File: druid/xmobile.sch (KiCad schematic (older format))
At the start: 10 parts, among them P3 CONN_8

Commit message: some changes
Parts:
- added J?: TP_VIBRO, symbol TEST_2P
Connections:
- wire segments 69 -> 70
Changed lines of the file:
@@
 	0    1    1    0
 $EndComp
+$Comp
+L TEST_2P J?
+U 1 1 5C561693
+P 7300 7200
+F 0 "J?" H 7300 7260 50  0000 C CNN
+F 1 "TP_VIBRO" H 7300 7130 50  0000 C CNN
+F 2 "" H 7300 7200 50  0001 C CNN
+F 3 "" H 7300 7200 50  0001 C CNN
+	1    7300 7200
+	1    0    0    -1
+$EndComp
+Wire Wire Line
+	7500 7200 7800 7200
+Text Label 7100 7200 2    60   ~ 0
+GND
 $EndSCHEMATC

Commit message: Add some packages
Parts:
- removed J?: Conn_01x04, symbol Conn_01x04
- added W?: TEST_PDI, Measurement_Points:Test_Point_2Pads, symbol TEST
- added W?: TEST_XMEGA_PWR, Measurement_Points:Test_Point_2Pads, symbol TEST
- C?: footprint (none) -> Capacitors_SMD:C_0402; case (none) -> 0402 In; example (none) -> https://eu.mouser.com/ProductDetail/AVX/04026D104KAT4A?qs=s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
- C?: value 10-100u -> 33u; footprint (none) -> Capacitors_SMD:c_elec_5x5.3; case (none) -> 5x5,3mm; example (none) -> https://eu.mouser.com/ProductDetail/Panasonic/EEE-0JA330WR?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
- J?: value TP_DISP_DATA_OUT -> TEST_DISP_DATA_OUT; footprint (none) -> Measurement_Points:Measurement_Point_Square-TH_Small; case (none) -> 1 pad
- J?: value TP_VIBRO -> TEST_VIBRO; footprint (none) -> Measurement_Points:Test_Point_2Pads; case (none) -> 2 pads
- P3: footprint Connectors_JAE:JAE_LY20-08P-2T_2x04x2.00mm_Straight -> Pin_Headers:Pin_Header_Straight_1x08
- R6: footprint (none) -> Resistors_SMD:R_0402; case (none) -> 0402 In; example (none) -> https://eu.mouser.com/ProductDetail/ROHM-Semiconductor/SFR0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
- SW?: case (none) -> 4x4x0,8; example (none) -> https://ru.aliexpress.com/item/100-4-4-0-8/32909011951.html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
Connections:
- wire segments 70 -> 69
- no-connect marks 3 -> 25
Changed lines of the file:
@@
 F 0 "R6" V 10105 10100 40  0000 C CNN
 F 1 "10k" V 10032 10101 40  0000 C CNN
-F 2 "" V 9955 10100 30  0000 C CNN
-F 3 "" H 10025 10100 30  0000 C CNN
+F 2 "Resistors_SMD:R_0402" V 9955 10100 30  0001 C CNN
+F 3 "https://eu.mouser.com/datasheet/2/348/sfr-e-1507454.pdf" V 10200 9750 30  0001 C CNN
+F 4 "https://eu.mouser.com/ProductDetail/ROHM-Semiconductor/SFR01MZPJ103?qs=sGAEpiMZZMtlubZbdhIBIIR71ikvQRXLchgEzboAcvI%3d" V 10025 10100 60  0001 C CNN "example"
+F 5 "0402 In" V 9950 10100 30  0000 C CNN "case"
 	1    10025 10100
 	0    -1   -1   0
@@
 F 0 "P3" V 13475 7500 60  0000 C CNN
 F 1 "CONN_8" V 13575 7500 60  0000 C CNN
-F 2 "Connectors_JAE:JAE_LY20-08P-2T_2x04x2.00mm_Straight" H 13525 7500 60  0001 C CNN
+F 2 "Pin_Headers:Pin_Header_Straight_1x08" V 13700 7450 60  0000 C CNN
 F 3 "" H 13525 7500 60  0001 C CNN
-F 4 "EPD display connector" V 13700 7500 60  0000 C CNN "description"
+F 4 "EPD display connector" V 13700 7500 60  0001 C CNN "description"
 	1    13525 7500
 	1    0    0    -1
@@
 F1 "xmega_power.sch" 60
 $EndSheet
-Text Label 9650 10700 1    60   ~ 0
+Text Label 9725 10700 0    60   ~ 0
 3.3V
-Text Label 9450 10700 1    60   ~ 0
+Text Label 9325 10700 2    60   ~ 0
 GND
 Text Label 8700 10100 2    60   ~ 0
@@
 F4 "INT" O L 13125 6400 60
 $EndSheet
-Text Label 9975 10325 0    60   ~ 0
+Text Label 10100 10350 0    60   ~ 0
 PDI_D
 Text Label 9550 9950 1    60   ~ 0
@@
 Wire Wire Line
 	9300 10100 9775 10100
-Wire Wire Line
-	9550 9950 9550 10700
 Connection ~ 9550 10100
-Wire Wire Line
-	9750 10325 9750 10700
-Wire Wire Line
-	9750 10325 9975 10325
 Wire Wire Line
 	12875 4675 14025 4675
@@
 P 11625 4600
 F 0 "J?" H 11625 4870 50  0000 C CNN
-F 1 "TP_DISP_DATA_OUT" H 11625 4800 50  0000 C CNN
-F 2 "" H 11825 4600 50  0001 C CNN
+F 1 "TEST_DISP_DATA_OUT" H 11625 4800 50  0000 C CNN
+F 2 "Measurement_Points:Measurement_Point_Square-TH_Small" H 11650 4925 50  0001 C CNN
 F 3 "" H 11825 4600 50  0001 C CNN
+F 4 "1 pad" H 11625 4925 30  0000 C CNN "case"
 	1    11625 4600
 	0    1    1    0
@@
 P 1975 9100
 F 0 "C?" H 2000 9200 50  0000 L CNN
-F 1 "0.1u" H 2000 9000 50  0000 L CNN
-F 2 "" H 2150 9075 50  0000 C CNN
-F 3 "" H 1975 9100 50  0001 C CNN
+F 1 "0.1u" H 2100 9100 50  0000 L CNN
+F 2 "Capacitors_SMD:C_0402" H 2175 9375 50  0001 C CNN
+F 3 "https://eu.mouser.com/datasheet/2/40/cx5r-776519.pdf" H 1975 9100 50  0001 C CNN
+F 4 "https://eu.mouser.com/ProductDetail/AVX/04026D104KAT4A?qs=sGAEpiMZZMs0AnBnWHyRQPg4iYkCw7IMED%2f4kpqgf7w%3d" H 1975 9100 60  0001 C CNN "example"
+F 5 "0402 In" H 2100 9025 30  0000 C CNN "case"
 	1    1975 9100
 	1    0    0    -1
@@
 P 1650 9100
 F 0 "C?" H 1675 9200 50  0000 L CNN
-F 1 "10-100u" H 1275 9000 50  0000 L CNN
-F 2 "" H 1475 9000 50  0000 C CNN
-F 3 "" H 1650 9100 50  0001 C CNN
+F 1 "33u" H 1400 9100 50  0000 L CNN
+F 2 "Capacitors_SMD:c_elec_5x5.3" H 1200 8875 50  0001 C CNN
+F 3 "https://eu.mouser.com/datasheet/2/315/ABA0000C1145-947633.pdf" H 1650 9100 50  0001 C CNN
+F 4 "https://eu.mouser.com/ProductDetail/Panasonic/EEE-0JA330WR?qs=sGAEpiMZZMsh%252b1woXyUXj65gIueAj9S3%2f2x%2f8oLKGVE%3d" H 1650 9100 60  0001 C CNN "example"
+F 5 "5x5,3mm" H 1525 9025 30  0000 C CNN "case"
 	1    1650 9100
 	1    0    0    -1
@@
 F 0 "SW?" H 9150 10210 50  0000 C CNN
 F 1 "SW_PUSH" H 9000 10020 50  0000 C CNN
-F 2 "druid:button_4pin_7,5x5" H 8975 9950 50  0000 C CNN
+F 2 "druid:button_4pin_7,5x5" H 8975 9950 50  0001 C CNN
 F 3 "" H 9000 10100 50  0000 C CNN
+F 4 "https://ru.aliexpress.com/item/100-4-4-0-8/32909011951.html?spm=a2g0v.search0604.3.313.5a9f5cbe3LNMTR&ws_ab_test=searchweb0_0%2Csearchweb201602_6_10065_10068_319_317_10696_10084_453_10083_454_10618_10304_10307_10820_10821_10301_537_536_10902_10843_10059_10884_10887_321_322_10103%2Csearchweb201603_51%2CppcSwitch_0&algo_pvid=b432da11-c10a-421f-96ee-7905deee8d06&algo_expid=b432da11-c10a-421f-96ee-7905deee8d06-45" H 9000 10100 60  0001 C CNN "example"
+F 5 "4x4x0,8" H 9000 10100 30  0000 C CNN "case"
 	1    9000 10100
 	1    0    0    -1
-$EndComp
-$Comp
-L Conn_01x04 J?
-U 1 1 5C50A6E4
-P 9650 10900
-F 0 "J?" H 9650 11100 50  0000 C CNN
-F 1 "Conn_01x04" V 9750 10850 50  0000 C CNN
-F 2 "" H 9650 10900 50  0001 C CNN
-F 3 "" H 9650 10900 50  0001 C CNN
-	1    9650 10900
-	0    1    1    0
 $EndComp
 $Comp
@@
 P 7300 7200
 F 0 "J?" H 7300 7260 50  0000 C CNN
-F 1 "TP_VIBRO" H 7300 7130 50  0000 C CNN
-F 2 "" H 7300 7200 50  0001 C CNN
+F 1 "TEST_VIBRO" H 7300 7130 50  0000 C CNN
+F 2 "Measurement_Points:Test_Point_2Pads" H 6925 7025 50  0001 C CNN
 F 3 "" H 7300 7200 50  0001 C CNN
+F 4 "2 pads" H 7300 7075 30  0000 C CNN "case"
 	1    7300 7200
 	1    0    0    -1
@@
 Text Label 7100 7200 2    60   ~ 0
 GND
+$Comp
+L TEST W?
+U 1 1 5C6C0FE4
+P 9900 10350
+F 0 "W?" H 9900 10410 50  0000 C CNN
+F 1 "TEST_PDI" H 9900 10280 50  0000 C CNN
+F 2 "Measurement_Points:Test_Point_2Pads" H 10150 10200 50  0001 C CNN
+F 3 "" H 9900 10350 50  0000 C CNN
+F 4 "2 pads" H 9900 10225 30  0000 C CNN "case"
+	1    9900 10350
+	1    0    0    -1
+$EndComp
+$Comp
+L TEST W?
+U 1 1 5C6C18FA
+P 9525 10700
+F 0 "W?" H 9525 10760 50  0000 C CNN
+F 1 "TEST_XMEGA_PWR" H 9525 10630 50  0000 C CNN
+F 2 "Measurement_Points:Test_Point_2Pads" H 9625 10550 50  0001 C CNN
+F 3 "" H 9525 10700 50  0000 C CNN
+F 4 "2 pads" H 9525 10575 30  0000 C CNN "case"
+	1    9525 10700
+	1    0    0    -1
+$EndComp
+Wire Wire Line
+	9550 10350 9700 10350
+Wire Wire Line
+	9550 9950 9550 10350
+NoConn ~ 10800 4900
+NoConn ~ 10800 5000
+NoConn ~ 10800 5400
+NoConn ~ 10800 5500
+NoConn ~ 10800 5600
+NoConn ~ 10800 5700
+NoConn ~ 10800 5800
+NoConn ~ 10800 5900
+NoConn ~ 10800 6000
+NoConn ~ 10800 6100
+NoConn ~ 10800 6300
+NoConn ~ 10800 6400
+NoConn ~ 10800 6500
+NoConn ~ 10800 7400
+NoConn ~ 10800 7500
+NoConn ~ 10800 7600
+NoConn ~ 10800 7700
+NoConn ~ 7800 7300
+NoConn ~ 7800 7400
+NoConn ~ 7800 7500
+NoConn ~ 7800 7700
+NoConn ~ 7800 7800
 $EndSCHEMATC

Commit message: Add packages for LEDs
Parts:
- W? (x2): symbol TEST -> TEST-RESCUE-xmobile
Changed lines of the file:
@@
 GND
 $Comp
-L TEST W?
+L TEST-RESCUE-xmobile W?
 U 1 1 5C6C0FE4
 P 9900 10350
@@
 $EndComp
 $Comp
-L TEST W?
+L TEST-RESCUE-xmobile W?
 U 1 1 5C6C18FA
 P 9525 10700

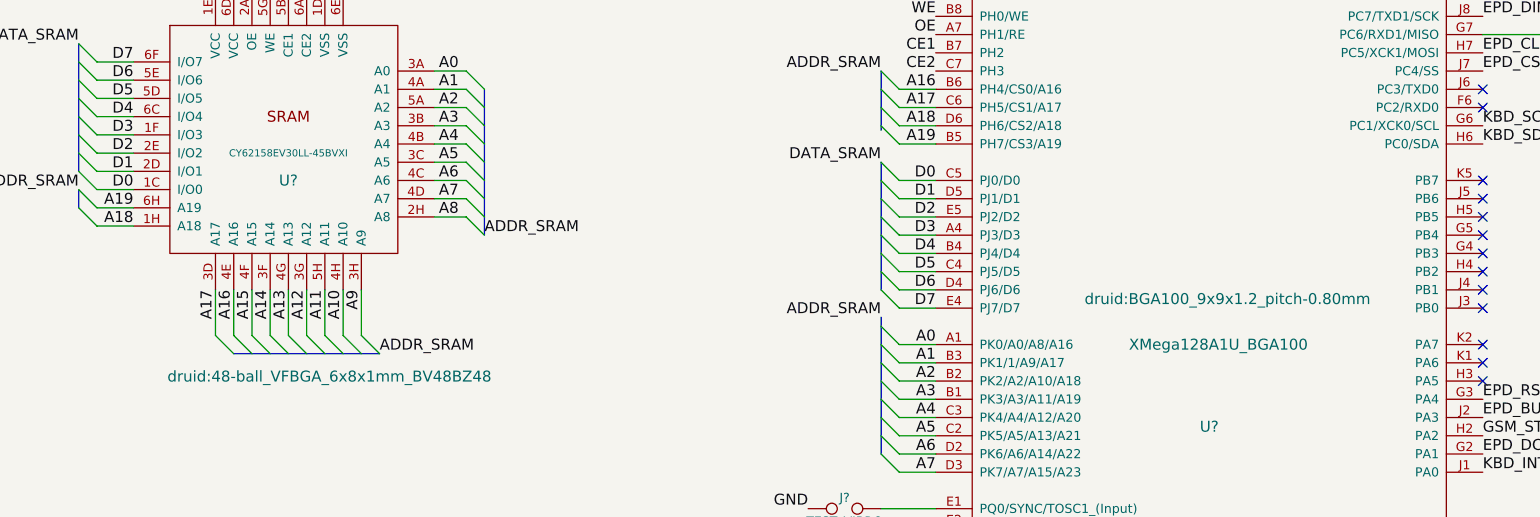
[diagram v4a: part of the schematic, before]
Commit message: Add packages: power module completed. Add packages: keyboard module completed.
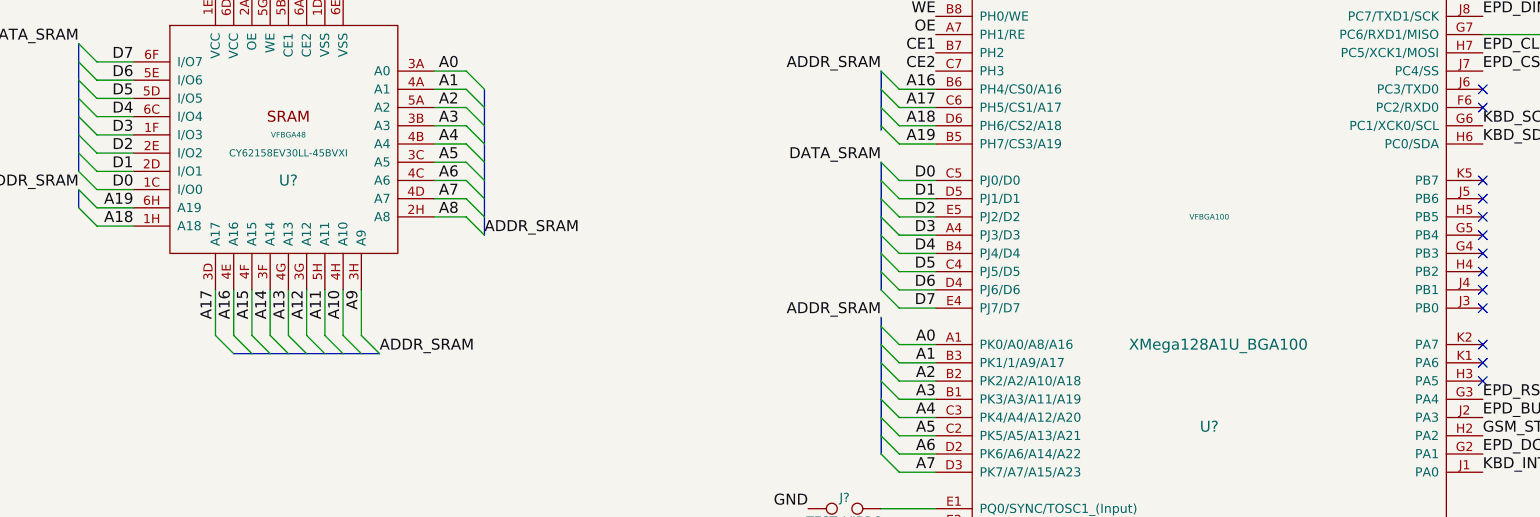
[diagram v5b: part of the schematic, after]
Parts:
- U?: case (none) -> VFBGA48; example (none) -> https://eu.mouser.com/ProductDetail/Cypress-Semiconductor/C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
- U?: case (none) -> VFBGA100; example (none) -> https://eu.mouser.com/ProductDetail/Microchip-Technology-At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
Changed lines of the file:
@@
 F 0 "U?" H 4250 5000 60  0000 C CNN
 F 1 "CY62158EV30LL-45BVXI" H 4250 5150 39  0000 C CNN
-F 2 "druid:48-ball_VFBGA_6x8x1mm_BV48BZ48" H 4475 3925 60  0000 C CNN
-F 3 "" H 4300 4250 60  0000 C CNN
+F 2 "druid:48-ball_VFBGA_6x8x1mm_BV48BZ48" H 4475 3925 60  0001 C CNN
+F 3 "https://www.cypress.com/file/43811/download" H 4300 4250 60  0001 C CNN
+F 4 "VFBGA48" H 4250 5250 30  0000 C CNN "case"
+F 5 "https://eu.mouser.com/ProductDetail/Cypress-Semiconductor/CY62158EV30LL-45BVXI?qs=sGAEpiMZZMt9mBA6nIyysIT6PXTPi%2fj%2fhnigerrGPws%3d" H 4250 5200 60  0001 C CNN "example"
 	1    4250 5200
 	1    0    0    -1
@@
 F 0 "U?" H 9300 4450 60  0000 C CNN
 F 1 "XMega128A1U_BGA100" H 9350 4900 60  0000 C CNN
-F 2 "druid:BGA100_9x9x1.2_pitch-0.80mm" H 9400 5150 60  0000 C CNN
-F 3 "" H 9700 7400 60  0000 C CNN
+F 2 "druid:BGA100_9x9x1.2_pitch-0.80mm" H 9400 5150 60  0001 C CNN
+F 3 "https://eu.mouser.com/datasheet/2/268/Atmel-8385-8-and-16-bit-AVR-Microcontroller-ATxmeg-1315775.pdf" H 9700 7400 60  0001 C CNN
+F 4 "https://eu.mouser.com/ProductDetail/Microchip-Technology-Atmel/ATXMEGA128A1U-C7U?qs=sGAEpiMZZMvqv2n3s2xjsVQIURldyCCHGWx9j4DhqLs%3d" H 9300 5600 60  0001 C CNN "example"
+F 5 "VFBGA100" H 9300 5600 30  0000 C CNN "case"
 	1    9300 5600
 	1    0    0    -1

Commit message: move to kicad 5
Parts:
- C?: symbol C -> xmobile-rescue:C
- C?: symbol CP -> xmobile-rescue:CP
- J?: symbol TEST_1P -> xmobile-rescue:TEST_1P
- J?: symbol Micro_SD_Card -> xmobile-rescue:Micro_SD_Card
- J?: symbol TEST_2P -> xmobile-rescue:TEST_2P
- P3: symbol CONN_8 -> xmobile-rescue:CONN_8
- R6: symbol R-RESCUE-xmobile -> xmobile-rescue:R-RESCUE-xmobile
- SW?: symbol SW_PUSH -> xmobile-rescue:SW_PUSH
- U?: symbol CY62158EV30LL-45BVXI -> xmobile-rescue:CY62158EV30LL-45BVXI
- U?: symbol XMega128A1U_BGA100 -> xmobile-rescue:XMega128A1U_BGA100
- W? (x2): symbol TEST-RESCUE-xmobile -> xmobile-rescue:TEST-RESCUE-xmobile
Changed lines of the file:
@@
-EESchema Schematic File Version 2
-LIBS:xmobile-rescue
-LIBS:power
-LIBS:device
-LIBS:transistors
-LIBS:conn
-LIBS:linear
-LIBS:regul
-LIBS:74xx
-LIBS:cmos4000
-LIBS:adc-dac
-LIBS:memory
-LIBS:xilinx
-LIBS:microcontrollers
-LIBS:dsp
-LIBS:microchip
-LIBS:analog_switches
-LIBS:motorola
-LIBS:texas
-LIBS:intel
-LIBS:audio
-LIBS:interface
-LIBS:digital-audio
-LIBS:philips
-LIBS:display
-LIBS:cypress
-LIBS:siliconi
-LIBS:opto
-LIBS:atmel
-LIBS:contrib
-LIBS:valves
-LIBS:XC6206P332MR
-LIBS:STF202-22T1G
-LIBS:MCP73871
-LIBS:switch1
-LIBS:SRAM
-LIBS:xmega128a1u_bga100
-LIBS:sim-holders
-LIBS:max7370
-LIBS:tp4056
+EESchema Schematic File Version 4
 LIBS:xmobile-cache
-EELAYER 25 0
+EELAYER 26 0
 EELAYER END
 $Descr A3 16535 11693
@@
 $EndDescr
 $Comp
-L R-RESCUE-xmobile R6
+L xmobile-rescue:R-RESCUE-xmobile R6
 U 1 1 5967CB22
 P 10025 10100
@@
 3.3V
 $Comp
-L CONN_8 P3
+L xmobile-rescue:CONN_8 P3
 U 1 1 5974D7B3
 P 13525 7500
@@
 PDI_C
 $Comp
-L CY62158EV30LL-45BVXI U?
+L xmobile-rescue:CY62158EV30LL-45BVXI U?
 U 1 1 5C118522
 P 4250 5200
@@
 $EndComp
 $Comp
-L XMega128A1U_BGA100 U?
+L xmobile-rescue:XMega128A1U_BGA100 U?
 U 1 1 5C19D697
 P 9300 5600
@@
 3.3V
 Wire Wire Line
-	9300 10100 9775 10100
+	9300 10100 9550 10100
 Connection ~ 9550 10100
 Wire Wire Line
@@
 Wire Wire Line
 	7800 6100 7600 6100
-Wire Bus Line
-	7500 5300 7500 6000
 Wire Wire Line
 	7800 6300 7600 6300
@@
 Wire Wire Line
 	7800 7000 7600 7000
-Wire Bus Line
-	7500 6150 7500 6900
 Wire Wire Line
 	7800 5200 7600 5200
@@
 Wire Wire Line
 	7800 3600 7600 3600
-Wire Bus Line
-	7500 4800 7500 5125
-Wire Bus Line
-	7500 3500 7500 4200
 Wire Wire Line
 	3400 5450 3200 5450
@@
 	3400 5650 3200 5650
 Wire Bus Line
-	5325 4900 5325 5700
-Wire Bus Line
-	3950 6350 4750 6350
-Wire Bus Line
-	3100 5350 3100 4650
-Wire Bus Line
 	3100 5550 3100 5450
 Wire Wire Line
-	8600 3100 9500 3100
+	8600 3100 8700 3100
 Connection ~ 8700 3100
 Connection ~ 8800 3100
@@
 KBD_INT
 $Comp
-L TEST_1P J?
+L xmobile-rescue:TEST_1P J?
 U 1 1 5C4B9CCC
 P 11625 4600
@@
 GSM_STATUS
 $Comp
-L Micro_SD_Card J?
+L xmobile-rescue:Micro_SD_Card J?
 U 1 1 5C4DB2CD
 P 4075 8950
@@
 GND
 $Comp
-L C C?
+L xmobile-rescue:C C?
 U 1 1 5C4DFD85
 P 1975 9100
@@
 $EndComp
 $Comp
-L CP C?
+L xmobile-rescue:CP C?
 U 1 1 5C4DFEA4
 P 1650 9100
@@
 $EndComp
 Wire Wire Line
-	1650 8950 3175 8950
-Wire Wire Line
-	1650 9250 1975 9250
+	1650 8950 1975 8950
+Wire Wire Line
+	1650 9250 1825 9250
 Wire Wire Line
 	1825 9525 1825 9250
@@
 microSD_CS
 $Comp
-L SW_PUSH SW?
+L xmobile-rescue:SW_PUSH SW?
 U 1 1 5C505516
 P 9000 10100
@@
 $EndComp
 $Comp
-L TEST_2P J?
+L xmobile-rescue:TEST_2P J?
 U 1 1 5C561693
 P 7300 7200
@@
 GND
 $Comp
-L TEST-RESCUE-xmobile W?
+L xmobile-rescue:TEST-RESCUE-xmobile W?
 U 1 1 5C6C0FE4
 P 9900 10350
@@
 $EndComp
 $Comp
-L TEST-RESCUE-xmobile W?
+L xmobile-rescue:TEST-RESCUE-xmobile W?
 U 1 1 5C6C18FA
 P 9525 10700
@@
 	9550 10350 9700 10350
 Wire Wire Line
-	9550 9950 9550 10350
+	9550 9950 9550 10100
 NoConn ~ 10800 4900
 NoConn ~ 10800 5000
@@
 NoConn ~ 7800 7700
 NoConn ~ 7800 7800
+Wire Wire Line
+	9550 10100 9775 10100
+Wire Wire Line
+	9550 10100 9550 10350
+Wire Wire Line
+	8700 3100 8800 3100
+Wire Wire Line
+	8800 3100 8900 3100
+Wire Wire Line
+	8900 3100 9000 3100
+Wire Wire Line
+	9000 3100 9100 3100
+Wire Wire Line
+	9100 3100 9200 3100
+Wire Wire Line
+	9200 3100 9300 3100
+Wire Wire Line
+	9300 3100 9400 3100
+Wire Wire Line
+	9400 3100 9500 3100
+Wire Wire Line
+	1825 9250 1975 9250
+Wire Wire Line
+	1975 8950 3175 8950
+Wire Bus Line
+	7500 4800 7500 5125
+Wire Bus Line
+	7500 5300 7500 6000
+Wire Bus Line
+	7500 3500 7500 4200
+Wire Bus Line
+	3100 4650 3100 5350
+Wire Bus Line
+	7500 6150 7500 6900
+Wire Bus Line
+	5325 4900 5325 5700
+Wire Bus Line
+	3950 6350 4750 6350
 $EndSCHEMATC

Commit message: looks like all packages added.
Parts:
- J?: footprint microSD:microSD-noname -> Connector_Card:microSD_HC_Wuerth_693072010801; case (none) -> 8 pin microSD; example (none) -> https://eu.mouser.com/ProductDetail/Wurth-Electronics/69307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
- P3: footprint Pin_Headers:Pin_Header_Straight_1x08 -> Connector_Pin_Header_1.00mm:PinHeader_1x08_P1.00mm_Vertical; case (none) -> pin header 1.00mm
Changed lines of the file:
@@
 F 0 "P3" V 13475 7500 60  0000 C CNN
 F 1 "CONN_8" V 13575 7500 60  0000 C CNN
-F 2 "Pin_Headers:Pin_Header_Straight_1x08" V 13700 7450 60  0000 C CNN
+F 2 "Connector_Pin_Header_1.00mm:PinHeader_1x08_P1.00mm_Vertical" V 13700 7450 60  0001 C CNN
 F 3 "" H 13525 7500 60  0001 C CNN
 F 4 "EPD display connector" V 13700 7500 60  0001 C CNN "description"
+F 5 "pin header 1.00mm" V 13675 7500 30  0000 C CNN "case"
 	1    13525 7500
 	1    0    0    -1
@@
 F 0 "J?" H 3425 9550 50  0000 C CNN
 F 1 "Micro_SD_Card" H 4725 9550 50  0000 R CNN
-F 2 "microSD:microSD-noname" H 4075 8200 50  0000 C CNN
-F 3 "" H 4075 8950 50  0001 C CNN
+F 2 "Connector_Card:microSD_HC_Wuerth_693072010801" H 4075 8200 50  0001 C CNN
+F 3 "https://eu.mouser.com/datasheet/2/445/693072010801-336093.pdf" H 4075 8950 50  0001 C CNN
+F 4 "https://eu.mouser.com/ProductDetail/Wurth-Electronics/693072010801?qs=sGAEpiMZZMuJakaoiLiBpiVYNV8REXtFk03jtifiNMv8wsb977CC%2fA%3d%3d" H 4075 8950 50  0001 C CNN "example"
+F 5 "8 pin microSD" H 4350 8925 30  0000 C CNN "case"
 	1    4075 8950
 	1    0    0    -1
